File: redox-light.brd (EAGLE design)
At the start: 164 x 127 mm, 128 parts, among them IC36 STM32F103TXUX, X2 USBMICRO_B, X3 AUDIO-JACKSMD

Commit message: layout template
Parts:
- added IC38: 74HC595BQ, netcat:DHVQFN16
- added IC39: W25Q64FV, netcat:WSON8
- C2: device netcat:R0402 -> netcat:SMC_A
- moved C6 13.5 mm to (108.9, 90.9), turned to 0 degrees
- moved VD27 9.00 mm to (119.6, 44.7), turned to 90 degrees
- moved C1 8.85 mm to (9.98, 111.5), turned to 0 degrees
- moved C2 8.84 mm to (9.93, 119.6), turned to 0 degrees
- moved VD30 6.94 mm to (17.4, 19.1)
- moved R8 6.69 mm to (3.77, 115.7), turned to 0 degrees
- moved Q2 6.61 mm to (3.48, 112.9)
- moved C13 5.80 mm to (43.8, 119.4), turned to 180 degrees
- moved VD35 4.44 mm to (119.4, 10.6), turned to 0 degrees
- moved C14 4.17 mm to (47.1, 116.8), turned to 90 degrees
- moved VD28 3.77 mm to (130.8, 30.1), turned to 0 degrees
- moved QZ1 3.46 mm to (44.2, 117.1), turned to 0 degrees
- moved VD20 3.32 mm to (115.8, 67.5)
- moved VD13 3.31 mm to (115.8, 86.3)
- moved IC37 2.53 mm to (9.65, 115.5), turned to 270 degrees
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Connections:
- removed net N$35: C1.+, IC37.3, X2.VBUS
- new net FLASH_CS: IC36.29, IC39.1
- new net SPI_MISO: IC36.31, IC39.2
- new net SPI_MOSI: IC36.32, IC39.5
- new net SPI_SCL: IC36.30, IC39.6
- new net SR_CLK: IC36.16, IC38.11, IC38.12
- new net SR_CLR: IC36.17, IC38.10
- new net SR_D: IC36.15, IC38.14
- net !BL_EN: now also IC36.20; no longer IC36.32
- net 5V: now also C1.+, IC37.3, X2.VBUS
- net BL_SDI: now also IC36.14; no longer IC36.20
- net GND: now also C2.-, IC38.13, IC38.8, IC38.PAD, IC39.4; no longer C2.2
- net N$17: now also VD4.C; no longer VD4.A
- net N$18: now also VD3.C; no longer VD3.A
- net N$19: now also VD5.C; no longer VD5.A
- net N$20: now also VD6.C; no longer VD6.A
- net N$21: now also VD2.C; no longer VD2.A
- net N$22: now also VD13.C; no longer VD13.A
- net N$24: now also VD7.C; no longer VD7.A
- net N$25: now also VD8.C; no longer VD8.A
- net N$26: now also VD9.C; no longer VD9.A
- net N$27: now also VD10.C; no longer VD10.A
- net N$28: now also VD11.C; no longer VD11.A
- net N$29: now also VD12.C; no longer VD12.A
- net N$30: now also VD20.C; no longer VD20.A
- net N$46: now also VD14.C; no longer VD14.A
- net N$47: now also VD15.C; no longer VD15.A
- net N$48: now also VD16.C; no longer VD16.A
- net N$49: now also VD17.C; no longer VD17.A
- net N$50: now also VD18.C; no longer VD18.A
- net N$51: now also VD19.C; no longer VD19.A
- net N$54: now also VD21.C; no longer VD21.A
- net N$55: now also VD22.C; no longer VD22.A
- net N$56: now also VD29.C; no longer VD29.A
- net N$57: now also VD30.C; no longer VD30.A
- net N$58: now also VD23.C; no longer VD23.A
- net N$59: now also VD24.C; no longer VD24.A
- net N$60: now also VD25.C; no longer VD25.A
- net N$61: now also VD26.C; no longer VD26.A
- net N$62: now also VD27.C; no longer VD27.A
- net N$63: now also VD28.C; no longer VD28.A
- net N$64: now also VD31.C; no longer VD31.A
- net N$65: now also VD32.C; no longer VD32.A
- net N$66: now also VD33.C; no longer VD33.A
- net N$67: now also VD34.C; no longer VD34.A
- net N$68: now also VD35.C; no longer VD35.A
- net N$7: now also VD1.C; no longer VD1.A
- net ROW0: now also IC38.15, VD1.A, VD13.A, VD2.A, VD3.A, VD4.A, VD5.A, VD6.A; no longer IC36.15, VD1.C, VD13.C, VD2.C, VD3.C, VD4.C, VD5.C, VD6.C
- net ROW1: now also IC38.1, VD10.A, VD11.A, VD12.A, VD20.A, VD7.A, VD8.A, VD9.A; no longer IC36.16, VD10.C, VD11.C, VD12.C, VD20.C, VD7.C, VD8.C, VD9.C
- net ROW2: now also IC38.2, VD14.A, VD15.A, VD16.A, VD17.A, VD18.A, VD19.A, VD27.A; no longer IC36.17, VD14.C, VD15.C, VD16.C, VD17.C, VD18.C, VD19.C, VD27.C
- net ROW3: now also IC38.3, VD21.A, VD22.A, VD23.A, VD24.A, VD25.A, VD26.A, VD28.A; no longer IC36.30, VD21.C, VD22.C, VD23.C, VD24.C, VD25.C, VD26.C, VD28.C
- net ROW4: now also IC38.4, VD29.A, VD30.A, VD31.A, VD32.A, VD33.A, VD34.A, VD35.A; no longer IC36.31, VD29.C, VD30.C, VD31.C, VD32.C, VD33.C, VD34.C, VD35.C
- net VCC: now also C2.+, IC38.16, IC39.8; no longer C2.1
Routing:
- net VCC_LEDS: track 0.00 -> 836.1 mm, vias 0 -> 1
- net ROW4: track 0.00 -> 227.6 mm
- net ROW3: track 0.00 -> 227.1 mm
- net COL6: track 0.00 -> 207.0 mm
- net ROW2: track 0.00 -> 202.1 mm
- net ROW1: track 0.00 -> 174.2 mm
- net COL5: track 0.00 -> 171.4 mm, vias 0 -> 8
- net VCC: track 0.00 -> 159.0 mm, vias 0 -> 7
- net ROW0: track 0.00 -> 155.8 mm
- net COL4: track 0.00 -> 145.0 mm, vias 0 -> 8
- net COL3: track 0.00 -> 119.4 mm, vias 0 -> 8
- net COL0: track 0.00 -> 105.9 mm, vias 0 -> 8
- net COL2: track 0.00 -> 100.3 mm, vias 0 -> 8
- net I2C_SDA: track 0.00 -> 89.3 mm
- net COL1: track 0.00 -> 88.4 mm, vias 0 -> 8
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- added copper zone on layer 1, net GND
- added copper zone on layer 16, net GND

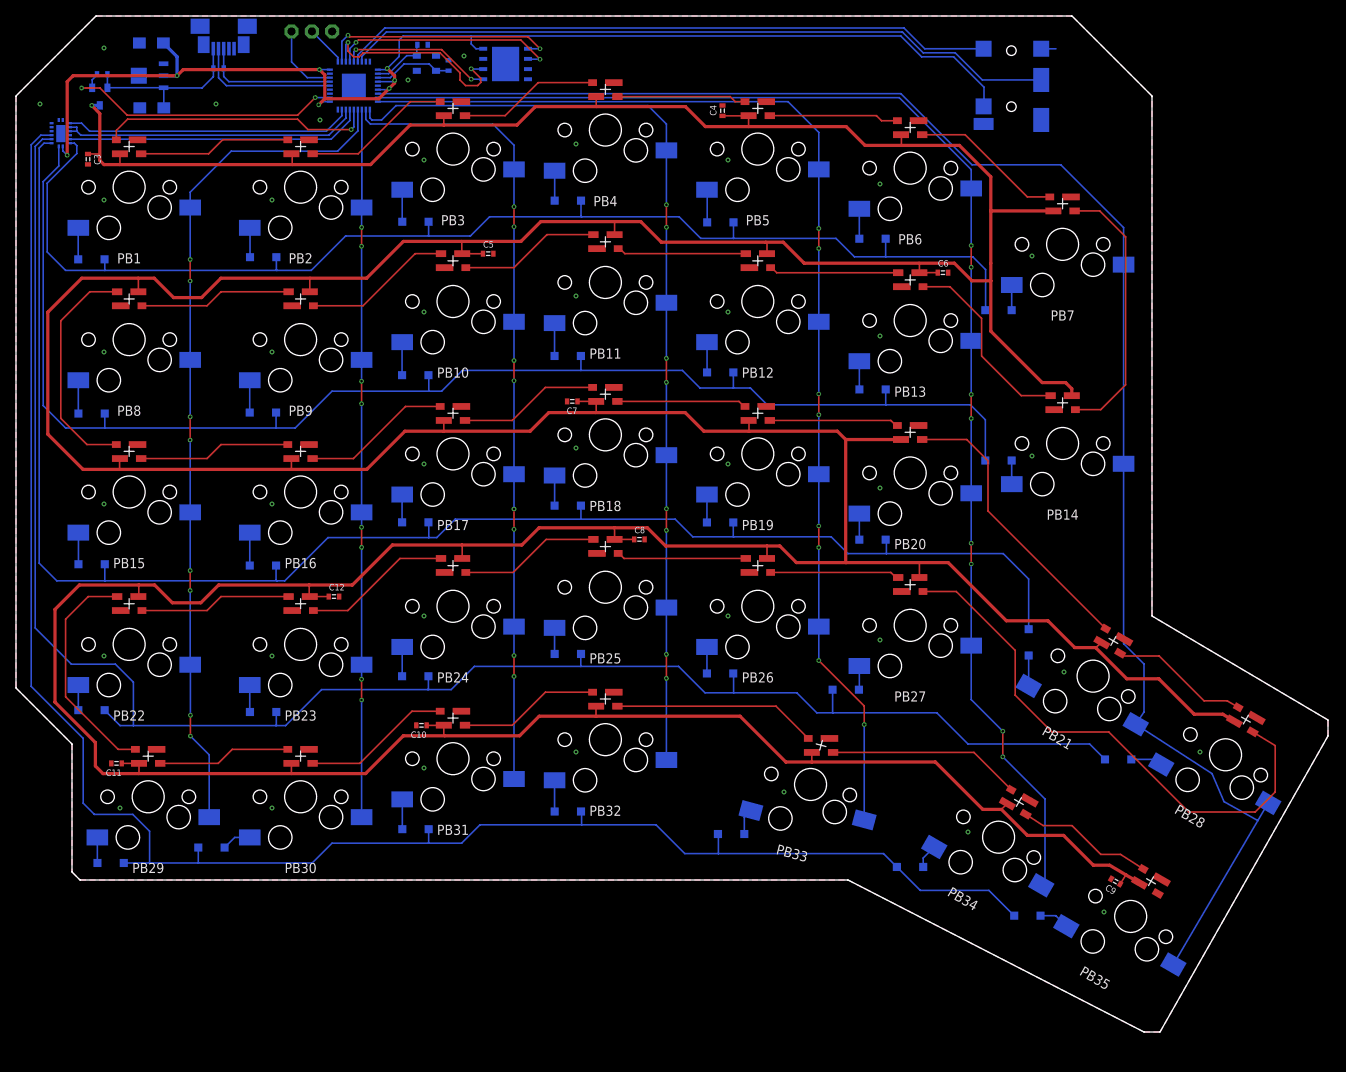
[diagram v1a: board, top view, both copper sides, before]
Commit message: aligned buttons, board layout completed
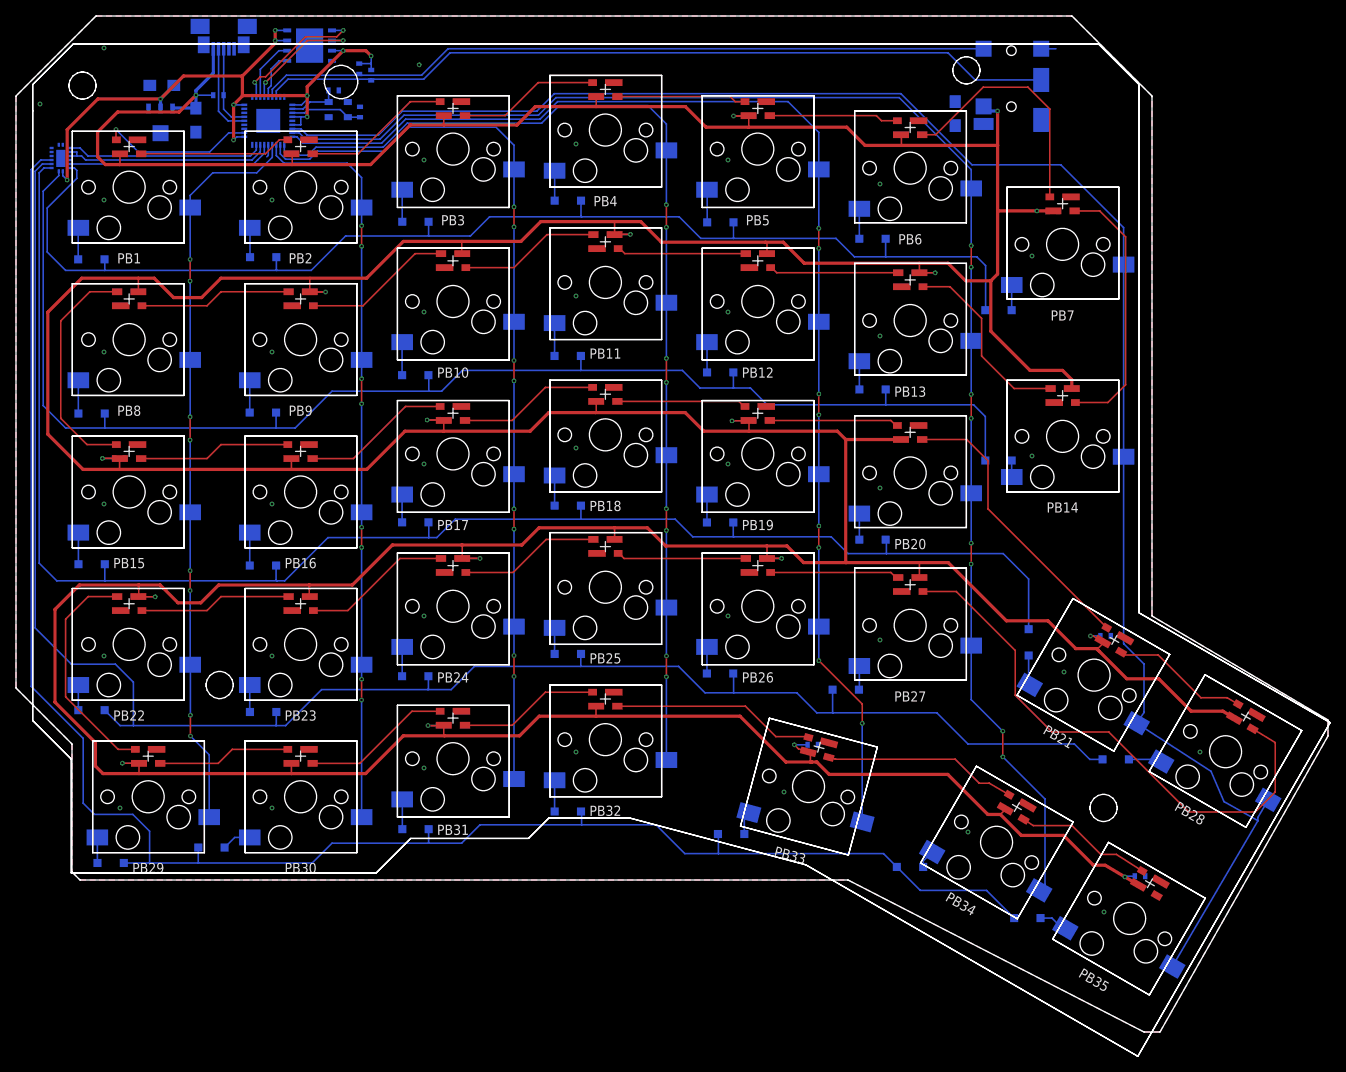
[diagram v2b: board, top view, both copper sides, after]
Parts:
- removed Q2: (no value), netcat:SOT23
- removed R8: 100k, netcat:R0402
- removed X3: AUDIO-JACKSMD, netcat:PJ-342
- removed X4: (no value), netcat:1X03
- added C15, C16, C17, C18, C20, C21: (no value), netcat:R0402
- added C19: (no value), netcat:SMC_A
- added R2, R3: 4.7k, netcat:R0402
- added X1: USBMICRO_B, netcat:USB_MICROB
- X2: value USBMICRO_B -> AUDIO-JACKSMD; device netcat:USB_MICROB -> netcat:PJ-342
- moved C14 108.8 mm to (129.2, 45.5), turned to 180 degrees
- moved C9 101.9 mm to (46.5, 72.5), flipped to the bottom, turned to 180 degrees
- moved X2 98.7 mm to (117.4, 115.5)
- moved C3 82.8 mm to (84.6, 110.5), flipped to the bottom, turned to 180 degrees
- moved C13 77.3 mm to (86.9, 55.2), turned to 0 degrees
- moved C8 65.8 mm to (5.90, 67.7), flipped to the bottom, turned to 180 degrees
- moved C10 55.9 mm to (84.6, 72.4), flipped to the bottom
- moved C7 46.2 mm to (105.9, 90.9), flipped to the bottom, turned to 0 degrees
- moved C4 43.2 mm to (122.6, 98.6), flipped to the bottom, turned to 180 degrees
- moved C6 41.3 mm to (67.8, 95.7), flipped to the bottom
- moved IC39 24.6 mm to (29.7, 119.3)
- moved C5 22.8 mm to (29.7, 88.5), flipped to the bottom
- moved C11 21.0 mm to (8.30, 50.4), flipped to the bottom, turned to 0 degrees
- moved C12 16.7 mm to (48.8, 55.2), flipped to the bottom
- moved QZ1 12.5 mm to (33.2, 111.3)
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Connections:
- removed net !BL_EN: IC36.20, Q2.1, R8.2
- removed net VCC_LEDS: C10.1, C11.1, C12.1, C3.1, C4.1, C5.1, C6.1, C7.1, C8.1, C9.1, IC1.VDD, IC10.VDD, IC11.VDD, IC12.VDD, IC13.VDD, IC14.VDD, IC15.VDD, IC16.VDD, IC17.VDD, IC18.VDD, IC19.VDD, IC2.VDD, IC20.VDD, IC21.VDD, IC22.VDD, IC23.VDD, IC24.VDD, IC25.VDD, IC26.VDD, IC27.VDD, IC28.VDD, IC29.VDD, IC3.VDD, IC30.VDD, IC31.VDD, IC32.VDD, IC33.VDD, IC34.VDD, IC35.VDD, IC4.VDD, IC5.VDD, IC6.VDD, IC7.VDD, IC8.VDD, IC9.VDD, Q2.3
- net 5V: now also C10.1, C11.1, C12.1, C13.1, C14.1, C15.1, C16.1, C17.1, C18.1, C3.1, C4.1, C5.1, C6.1, C7.1, C8.1, C9.1, IC1.VDD, IC10.VDD, IC11.VDD, IC12.VDD, IC13.VDD, IC14.VDD, IC15.VDD, IC16.VDD, IC17.VDD, IC18.VDD, IC19.VDD, IC2.VDD, IC20.VDD, IC21.VDD, IC22.VDD, IC23.VDD, IC24.VDD, IC25.VDD, IC26.VDD, IC27.VDD, IC28.VDD, IC29.VDD, IC3.VDD, IC30.VDD, IC31.VDD, IC32.VDD, IC33.VDD, IC34.VDD, IC35.VDD, IC4.VDD, IC5.VDD, IC6.VDD, IC7.VDD, IC8.VDD, IC9.VDD, X1.VBUS, X2.4; no longer Q2.2, R8.1, X2.VBUS
- net BL_SDI: now also IC36.20; no longer IC36.14
- net GND: now also C15.2, C16.2, C17.2, C18.2, C19.-, C20.2, C21.2, IC36.14, X1.6, X1.7, X1.8, X1.9, X1.GND, X2.1; no longer X2.6, X2.7, X2.8, X2.9, X2.GND, X3.1, X4.1
- net I2C_SCL: now also R2.2, X2.2; no longer X3.2
- net I2C_SDA: now also R3.2, X2.3; no longer X3.3
- net N$23: now also C20.1; no longer C13.1
- net N$31: now also C21.1; no longer C14.1
- net SWD_CLK: no longer X4.2
- net SWD_IO: no longer X4.3
- net USB_DM: now also X1.D-; no longer X2.D-
- net USB_DP: now also X1.D+; no longer X2.D+
- net VCC: now also IC39.3, IC39.7, R2.1, R3.1; no longer X3.4
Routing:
- net 5V: track 22.0 -> 891.7 mm, vias 0 -> 18
- net VCC_LEDS: track 836.1 -> 0.00 mm, vias 1 -> 0
- net VCC: track 159.0 -> 90.8 mm, vias 7 -> 10
- net !BL_EN: track 36.6 -> 0.00 mm, vias 2 -> 0
- net SPI_SCL: track 26.8 -> 7.77 mm, vias 2 -> 0
- net BL_SDI: track 34.3 -> 19.5 mm
- net COL5: track 171.4 -> 185.3 mm
- net COL6: track 207.0 -> 220.7 mm
- net COL0: track 105.9 -> 92.5 mm
- net COL4: track 145.0 -> 158.3 mm
- net SPI_MISO: track 28.4 -> 15.1 mm
- net SPI_MOSI: track 19.1 -> 6.07 mm, vias 2 -> 0
- net FLASH_CS: track 29.8 -> 17.1 mm
- net COL3: track 119.4 -> 131.9 mm
- net COL2: track 100.3 -> 112.4 mm
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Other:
- board size 164 x 127 mm -> 164.3 x 130 mm

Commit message: layout, outline, silk update
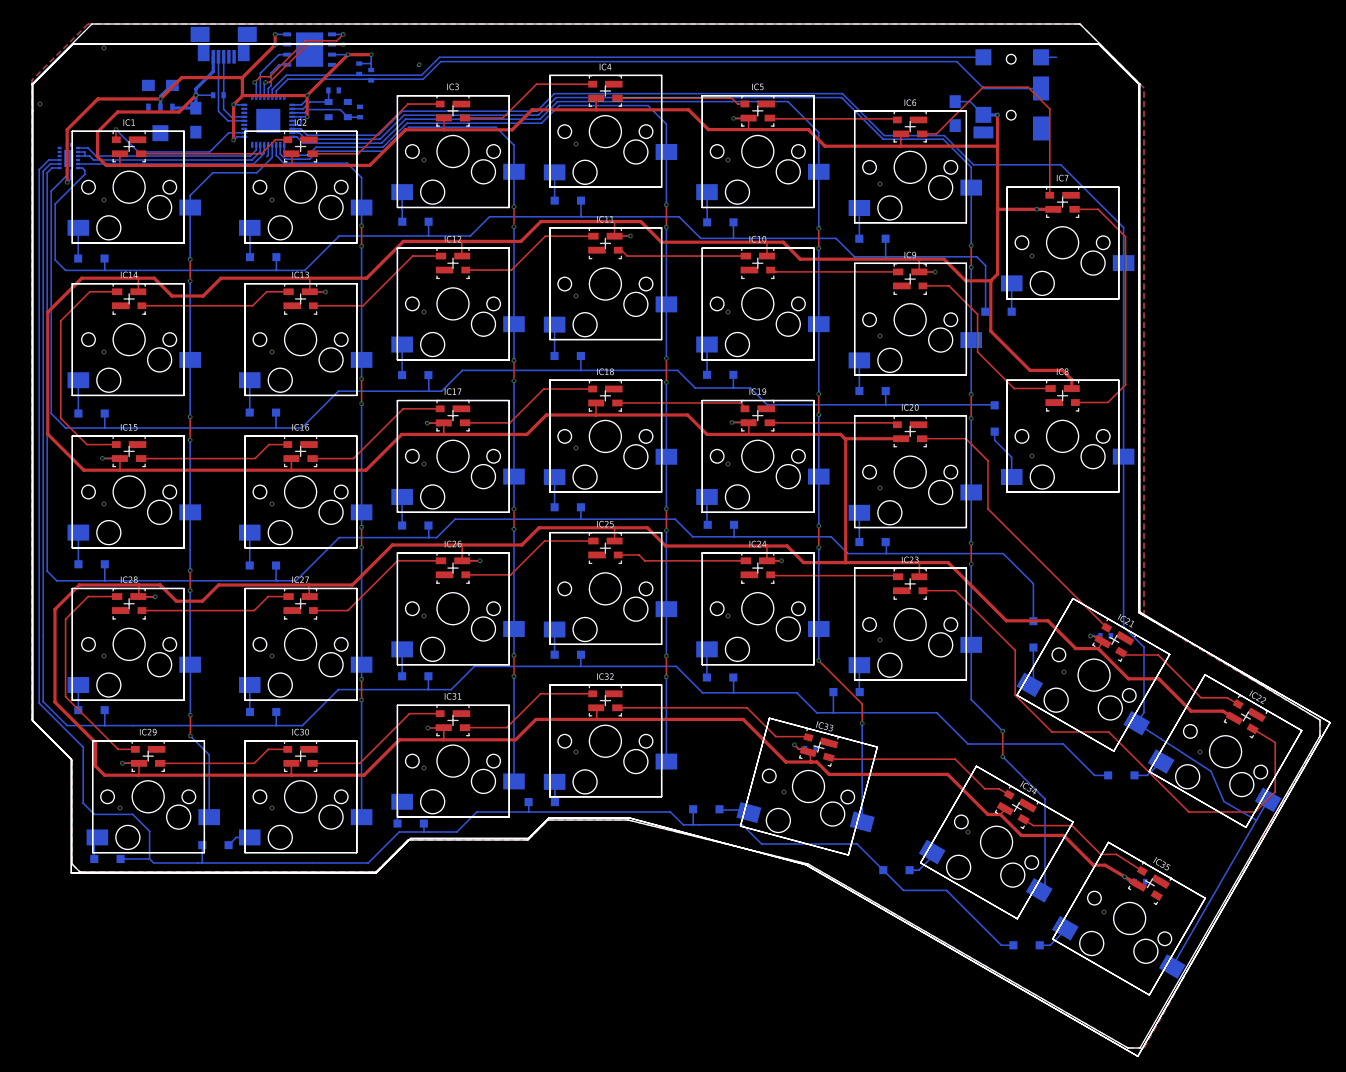
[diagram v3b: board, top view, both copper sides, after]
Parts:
- C1, C19: value (none) -> 10u
- C2: value (none) -> 4.7u
- moved VD20 5.24 mm to (115.4, 72.7), turned to 90 degrees
- moved VD33 4.38 mm to (79.3, 23.9)
- moved VD32 3.48 mm to (58.7, 24.8), turned to 0 degrees
- moved VD35 3.40 mm to (119.3, 6.86)
- moved VD28 2.12 mm to (131.2, 28.1)
- moved VD34 1.75 mm to (103.1, 16.3)
- moved VD27 1.17 mm to (120.2, 45.7)
- moved X2 1.07 mm to (117.4, 114.4)
- moved X1 1.00 mm to (19.0, 120.7)
- moved IC38 1.00 mm to (-0.40, 105.2)
- moved VD31 0.92 mm to (42.3, 22.0)
- moved C18 0.70 mm to (133.5, 14.8)
- moved VD29 0.64 mm to (4.43, 17.6)
- moved VD30 0.58 mm to (17.9, 19.4)
- moved C17 0.58 mm to (92.3, 31.4)
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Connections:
- net 5V: now also C19.+
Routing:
- net 5V: track 891.7 -> 898.1 mm
- net ROW1: track 171.4 -> 165.5 mm
- net N$30: track 2.07 -> 6.55 mm
- net ROW2: track 199.0 -> 196.6 mm
- net N$67: track 2.33 -> 4.12 mm
- net N$65: track 3.91 -> 2.63 mm
- net N$62: track 3.73 -> 4.87 mm
- net ROW4: track 224.6 -> 225.7 mm
- net USB_DP: track 10.5 -> 9.54 mm
- net USB_DM: track 11.5 -> 10.5 mm
- net SR_D: track 25.9 -> 24.9 mm
- net SR_CLR: track 24.7 -> 23.7 mm
- net SR_CLK: track 26.6 -> 25.6 mm
- net N$66: track 2.91 -> 3.85 mm
- net N$64: track 3.73 -> 2.97 mm
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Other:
- board size 164.3 x 130 mm -> 162.3 x 129 mm
